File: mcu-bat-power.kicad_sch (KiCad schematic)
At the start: 58 parts, among them IC1 CN3058E, IC2 HY2112, J1 USB_B_Micro, J2 INDICATORS, J3 PWR, J4 USB, J5 PWR, Q1 FS8205, Q2 2N7002, Q3 2N7002, SW1 SW_SPDT, U1 MT3608, U2 INA219AxD

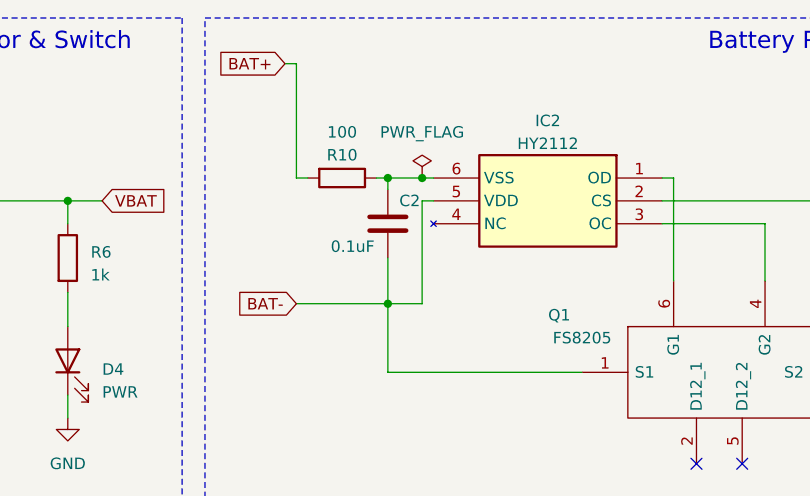
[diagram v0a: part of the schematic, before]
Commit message: Corrected VDD and VSS connection on HY chip
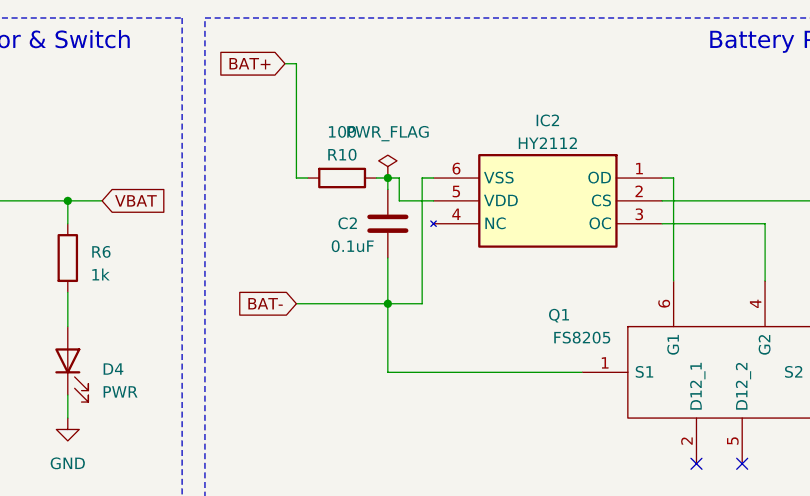
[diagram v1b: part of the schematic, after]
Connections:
- net BAT-: now also IC2.6 (VSS); no longer IC2.5 (VDD)
- net at C2.1, R10.1: now also IC2.5 (VDD); no longer IC2.6 (VSS)
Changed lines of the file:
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@@
 	)
 	(junction
+		(at 182.88 31.75)
+		(diameter 0)
+		(color 0 0 0 0)
+	)
+	(junction
 		(at 40.64 50.8)
 		(diameter 0)
@@
 	)
 	(junction
-		(at 186.69 31.75)
-		(diameter 0)
-		(color 0 0 0 0)
-	)
-	(junction
 		(at 148.59 137.16)
 		(diameter 0)
@@
 	)
 	(junction
-		(at 182.88 31.75)
-		(diameter 0)
-		(color 0 0 0 0)
-	)
-	(junction
 		(at 87.63 64.77)
 		(diameter 0)
@@
 	(wire
 		(pts
-			(xy 186.69 31.75) (xy 187.96 31.75)
-		)
-		(stroke
-			(width 0)
-			(type default)
-		)
-	)
-	(wire
-		(pts
 			(xy 147.32 44.45) (xy 147.32 48.26)
 		)
@@
 	(wire
 		(pts
-			(xy 182.88 31.75) (xy 186.69 31.75)
-		)
-		(stroke
-			(width 0)
-			(type default)
-		)
-	)
-	(wire
-		(pts
 			(xy 39.37 34.29) (xy 39.37 35.56)
 		)
@@
 	(wire
 		(pts
-			(xy 186.69 34.29) (xy 186.69 45.72)
+			(xy 186.69 31.75) (xy 186.69 45.72)
+		)
+		(stroke
+			(width 0)
+			(type default)
+		)
+	)
+	(wire
+		(pts
+			(xy 184.15 34.29) (xy 187.96 34.29)
 		)
 		(stroke
@@
 	(wire
 		(pts
+			(xy 186.69 31.75) (xy 187.96 31.75)
+		)
+		(stroke
+			(width 0)
+			(type default)
+		)
+	)
+	(wire
+		(pts
 			(xy 237.49 34.29) (xy 237.49 40.64)
 		)
@@
 	(wire
 		(pts
+			(xy 182.88 31.75) (xy 184.15 31.75)
+		)
+		(stroke
+			(width 0)
+			(type default)
+		)
+	)
+	(wire
+		(pts
 			(xy 231.14 132.08) (xy 231.14 129.54)
 		)
@@
 	(wire
 		(pts
+			(xy 184.15 31.75) (xy 184.15 34.29)
+		)
+		(stroke
+			(width 0)
+			(type default)
+		)
+	)
+	(wire
+		(pts
 			(xy 204.47 127) (xy 208.28 127)
 		)
@@
 	(wire
 		(pts
-			(xy 187.96 34.29) (xy 186.69 34.29)
-		)
-		(stroke
-			(width 0)
-			(type default)
-		)
-	)
-	(wire
-		(pts
 			(xy 116.84 64.77) (xy 116.84 49.53)
 		)
@@
 	(symbol
 		(lib_id "power:PWR_FLAG")
-		(at 186.69 31.75 0)
+		(at 182.88 31.75 0)
 		(unit 1)
 		(exclude_from_sim no)
@@
 		(fields_autoplaced yes)
 		(property "Reference" "#FLG02"
-			(at 186.69 29.845 0)
+			(at 182.88 29.845 0)
 			(effects
 				(font
@@
 		)
 		(property "Value" "PWR_FLAG"
-			(at 186.69 26.67 0)
+			(at 182.88 26.67 0)
 			(effects
 				(font
@@
 		)
 		(property "Footprint" ""
-			(at 186.69 31.75 0)
+			(at 182.88 31.75 0)
 			(effects
 				(font
@@
 		)
 		(property "Datasheet" "~"
-			(at 186.69 31.75 0)
+			(at 182.88 31.75 0)
 			(effects
 				(font
@@
 		)
 		(property "Description" ""
-			(at 186.69 31.75 0)
+			(at 182.88 31.75 0)
 			(effects
 				(font
@@
 		(dnp no)
 		(property "Reference" "C2"
-			(at 184.15 34.29 0)
+			(at 177.292 36.83 0)
 			(effects
 				(font
